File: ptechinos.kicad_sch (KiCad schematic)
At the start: 59 parts, among them J1 Bat_Pos, J2 Battery, J3 Bat_GND, J4 AudioJack4, SW1 SW_Power, SW2 Reset, U1 ProMicro

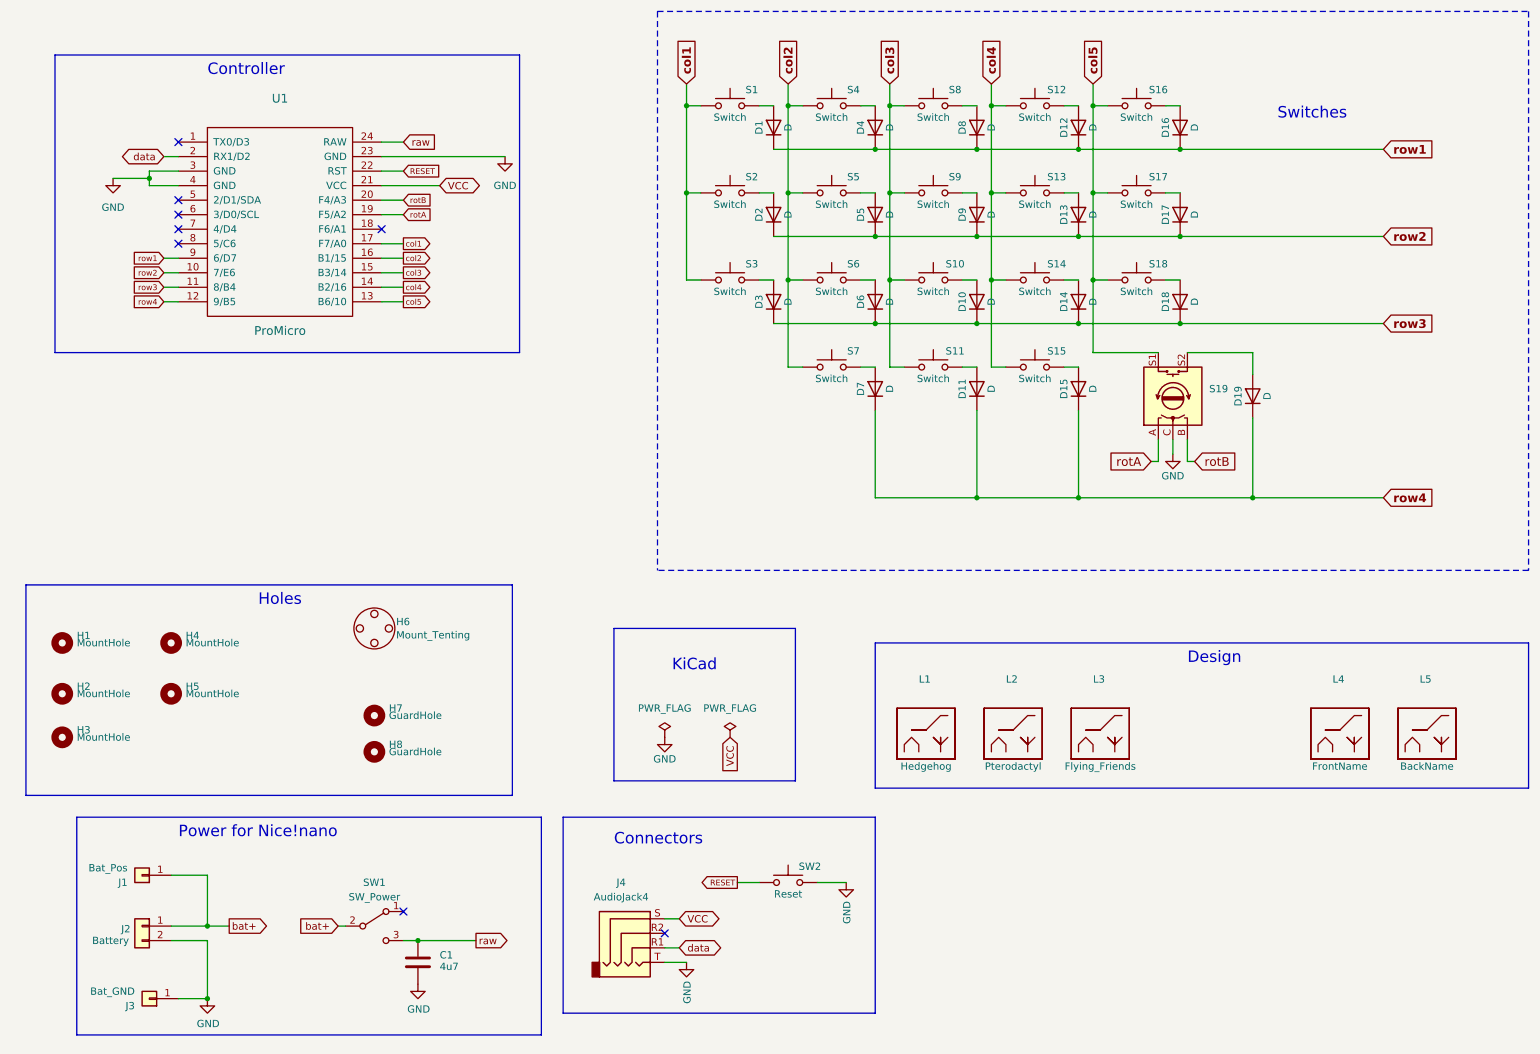
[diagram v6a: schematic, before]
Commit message: ✨ 🚧 - Update electric schema and PCB design to add support for Cirque trackpad. Clean / Improve routing. Still require some checks before being marked as completed. 1x12 connectors is still in early development and could be changed according to found pieces. Making space for all components is difficult and cleaning is required.
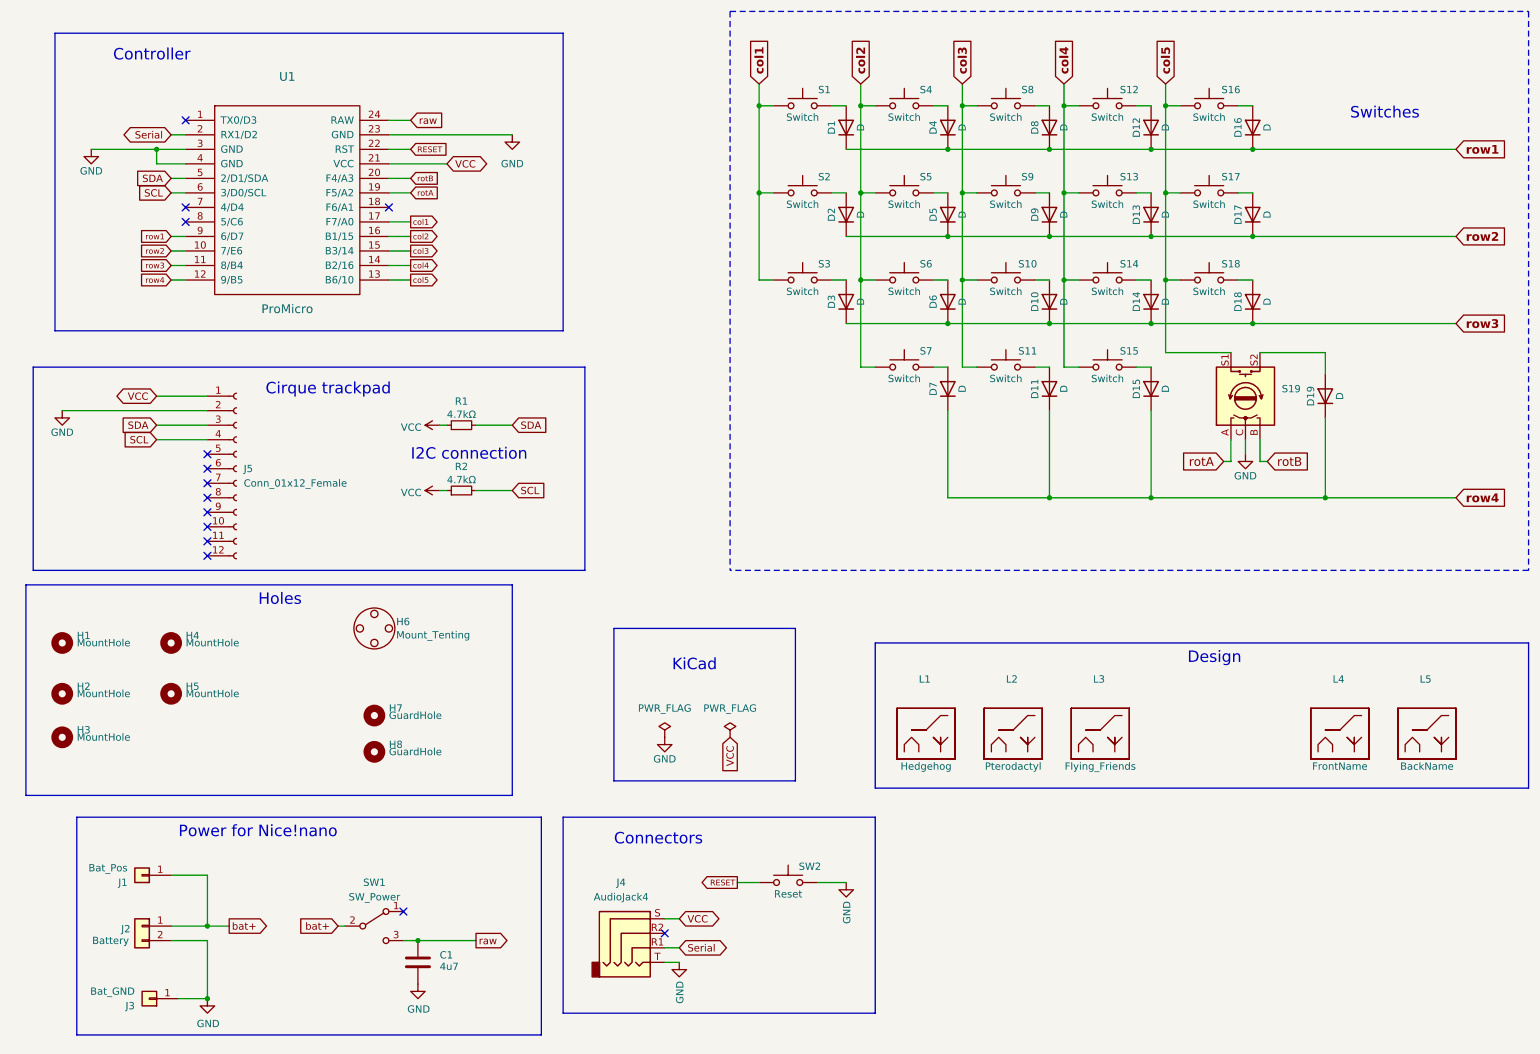
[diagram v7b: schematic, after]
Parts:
- added J5: Conn_01x12_Female, ptechinos:Molex_200528-0120_1x12-1MP_P1.00mm_Horizontal, symbol Connector:Conn_01x12_Female
- added R1, R2: 4.7kΩ, ptechinos:R_0805_2012Metric, symbol Device:R_Small
- H6: footprint ptechinos:Tenting_Puck_soft -> ptechinos:Tenting_Puck
- L1: footprint ptechinos:hedgehog-shadow-medium -> ptechinos-graphics:hedgehog-shadow-medium
- L2: footprint ptechinos:pterodactyl-shadow-medium -> ptechinos-graphics:pterodactyl-shadow-medium
- L3: footprint ptechinos:flying-friends-medium -> ptechinos-graphics:flying-friends-medium
- L4, L5: footprint ptechinos:board_name -> ptechinos-graphics:board_name
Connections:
- net GND: now also J5.2 (Pin_2)
- net VCC: now also J5.1 (Pin_1), R1.1, R2.1
- net SDA: now reaches U1.5 (2/D1/SDA)
- net SDA: now also J5.3 (Pin_3), R1.2
- net SCL: now reaches U1.6 (3/D0/SCL)
- net SCL: now also J5.4 (Pin_4), R2.2
- net data renamed Serial
- no-connect marks 8 -> 14
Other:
- note added: "Cirque trackpad"
- note added: "I2C connection"
- moved on the sheet: D1, D10, D11, D12, D13, D14, D15, D16, D17, D18, D19, D2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

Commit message: ✨ 🚧 - Update electric schema and PCB design to add support for both OLED and Cirque trackpad. Currently I2C connections are still pending but some space was created at the bottom of MCU.
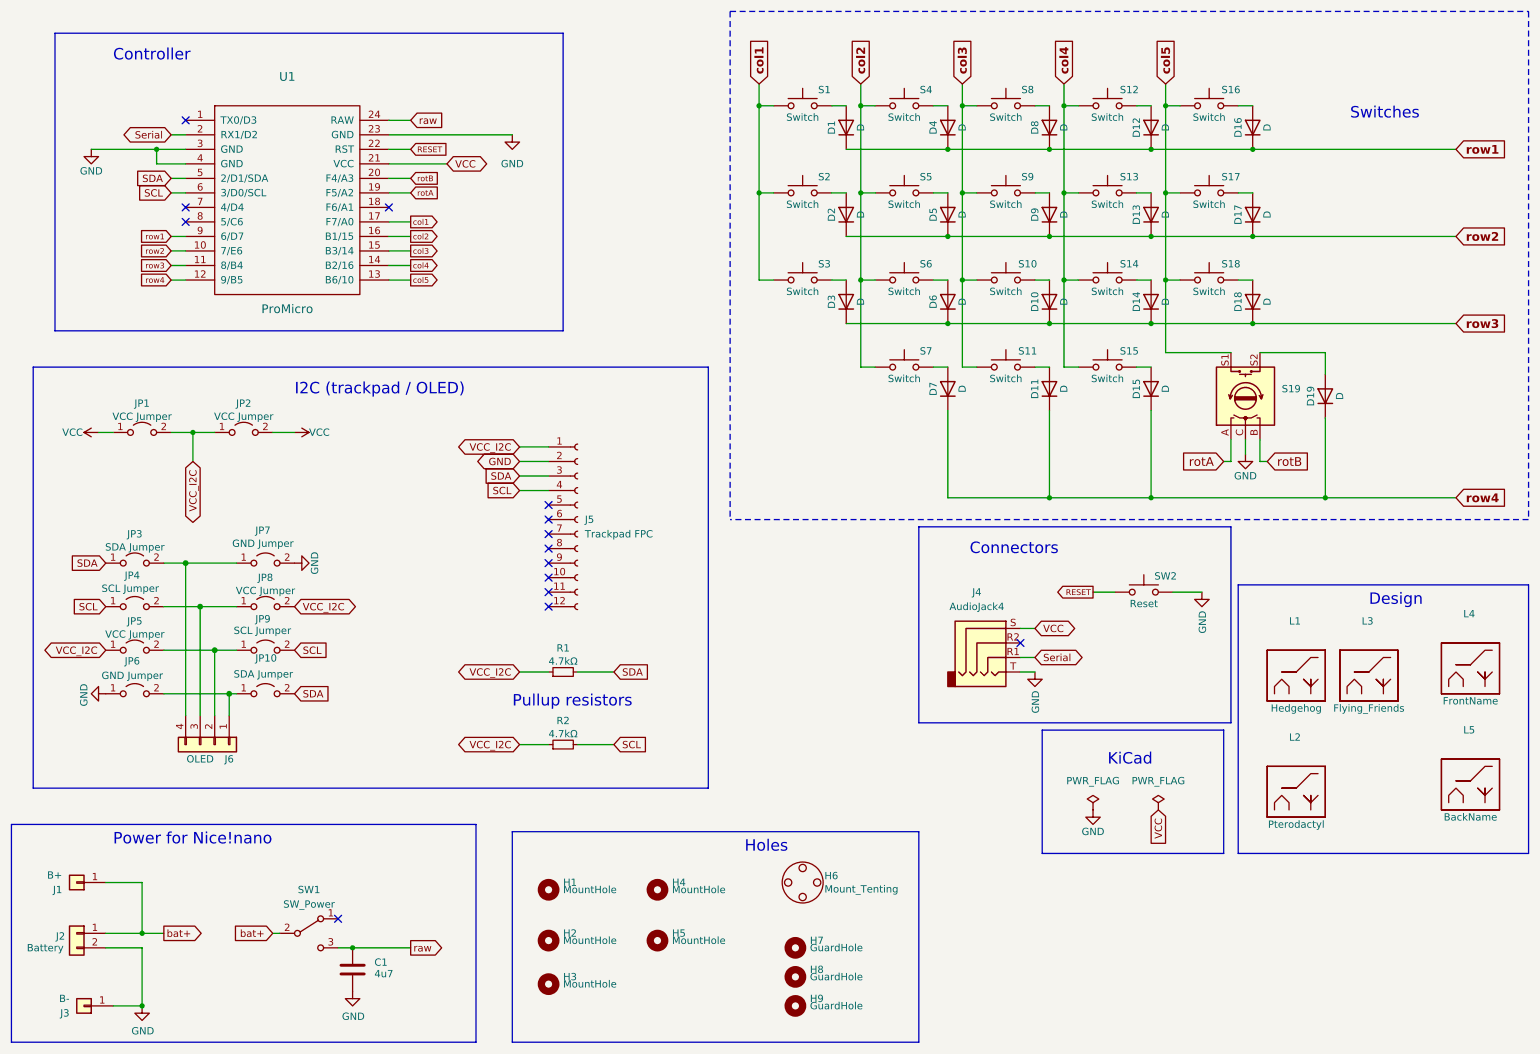
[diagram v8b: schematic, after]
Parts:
- added H9: GuardHole, ptechinos:M2_Guard_Hole, symbol Mechanical:MountingHole
- added J6: OLED, ptechinos:OLED, symbol Connector_Generic:Conn_01x04
- added JP1, JP2, JP5, JP8: VCC Jumper, ptechinos:Jumper_open, symbol Jumper:Jumper_2_Open
- added JP10, JP3: SDA Jumper, ptechinos:Jumper_open, symbol Jumper:Jumper_2_Open
- added JP4, JP9: SCL Jumper, ptechinos:Jumper_open, symbol Jumper:Jumper_2_Open
- added JP6, JP7: GND Jumper, ptechinos:Jumper_open, symbol Jumper:Jumper_2_Open
- J1: value Bat_Pos -> B+
- J3: value Bat_GND -> B-
- J5: value Conn_01x12_Female -> Trackpad FPC; footprint ptechinos:Molex_200528-0120_1x12-1MP_P1.00mm_Horizontal -> ptechinos:FPC-SMD_FPC05012-09200-.5mm-rev
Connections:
- net GND: now also JP6.1 (A), JP7.2 (B)
- net SCL: now also JP4.1 (A), JP9.2 (B)
- net SDA: now also JP10.2 (B), JP3.1 (A)
- net VCC: now also JP1.1 (A), JP2.2 (B); no longer J5.1 (Pin_1), R1.1, R2.1
- new net: J6.1 (Pin_1), JP10.1 (A), JP6.2 (B)
- new net: J6.4 (Pin_4), JP3.2 (B), JP7.1 (A)
- new net: J6.2 (Pin_2), JP5.2 (B), JP9.1 (A)
- new net: J6.3 (Pin_3), JP4.2 (B), JP8.1 (A)
- new net VCC_I2C: J5.1 (Pin_1), JP1.2 (B), JP2.1 (A), JP5.1 (A), JP8.2 (B), R1.1, R2.1
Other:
- note added: "I2C (trackpad / OLED)"
- note added: "Pullup resistors"
- note removed: "Cirque trackpad"
- note removed: "I2C connection"
- moved on the sheet: C1, H1, H2, H3, H4, H5, H6, H7, H8, J1, J2, J3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
